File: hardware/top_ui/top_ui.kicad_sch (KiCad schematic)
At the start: 25 parts, among them J1 USB-C, J2 J_STK_A, J3 J_STK_B, J5 ST7789 240x280, J6 Stern Klinke, J7 Reserve UART, Q1 BC847, Q2 P-FET 20V 1A, SW1 BTN1, SW2 BTN2, SW3 BTN3, SW4 BTN4, U1 USBLC6-2SC6, U2 SHT40-AD1B, U3 VL53L1X

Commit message: USB-C wandert auf das Mid-Board, Top bekommt eine Randkerbe
Der Grund ist Bauhoehe, nicht Routing. Ueber dem Top-Board sind bis zur
Zentralscheibe 3,5 mm frei; eine stehende USB-C-Buchse baut 7 bis 9,25 mm
(GCT USB4115: H = 9,25 mm laut Datenblatt). Sie haette die Scheibe
durchstossen. Zwischen Mids und Tops Oberseite liegen dagegen 10,0 mm.

Die Buchse steht jetzt auf Mid bei (3,5 / 20,3) und greift durch eine offene
Randkerbe des Top-Boards nach vorn - gesteckt wird weiterhin frontal, sobald
die Zentralscheibe ab ist. Koerper 8,3 x 4,3 mm, Kerbe 11,0 mm breit ab
y = 16,8 bis zum Rand.

Offene Kerbe statt Fenster, weil der Boardrand bei y = 23,5 liegt: Ein
geschlossenes Fenster liesse einen Steg von einem halben Millimeter stehen,
der beim Nutzentrennen bricht.

MITGEWANDERT sind die ESD-Diode (U5) und die beiden CC-Widerstaende
(R18/R19). Damit verlieren USB_DP und USB_DN ihren Weg durch den Stapel:
J_STK_A 34/36 heissen jetzt RSV_A3/RSV_A5. Der native USB des ESP32-S3 sitzt
auf demselben Board wie die Buchse. Stack-Pinout auf v0.4.

USB_VBUS bleibt auf A18 - es geht weiter nach unten zum Power-Mux auf Bottom,
kommt jetzt nur von Mid statt von Top.

PLATZIERUNG. Der Bodenrand von Mid war belegt: RS485 (J4) nach links auf
(-11,5 / 19,0) gerueckt, PhotoMOS (U4) aus der Fixliste genommen. Ein
Rastersuchlauf ueber beide Seiten fand fuer U4 keine freie Flaeche von
11,6 x 3,6 mm - der automatische Platzierer bringt ihn jetzt selbst unter und
hat ihn nach (-20,1 / 7,9) gelegt. Oben ging es nicht, dort steht das
ESP32-Modul mit seiner Antenne; links und rechts laesst Tops Displayfenster
nur 7,2 mm Rand.

inside_outline() kennt die Kerbe, der Platzierer legt dort nichts ab, und der
Zonenumriss folgt ihr.

  top_ui     27 -> 21 Bauteile, unrouted 63 -> 48
  mid_logic  46 -> 50 Bauteile

Co-Authored-By: Claude Opus 5 (1M context) <noreply@anthropic.com>
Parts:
- removed J1: USB-C, Connector_USB:USB_C_Receptacle_G-Switch_GT-USB-7051x, symbol Connector:USB_C_Receptacle_USB2.0_16P
- removed R1, R2: 5k1, Resistor_SMD:R_0603_1608Metric, symbol Device:R
- removed U1: USBLC6-2SC6, Package_TO_SOT_SMD:SOT-23-6, symbol Power_Protection:USBLC6-2SC6
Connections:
- net USB_DN renamed RSV_A5
- net USB_DP renamed RSV_A3
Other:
- moved on the sheet: C1, C2, C3, C4, F1, J2, J3, J5, J6, J7, Q1, Q2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

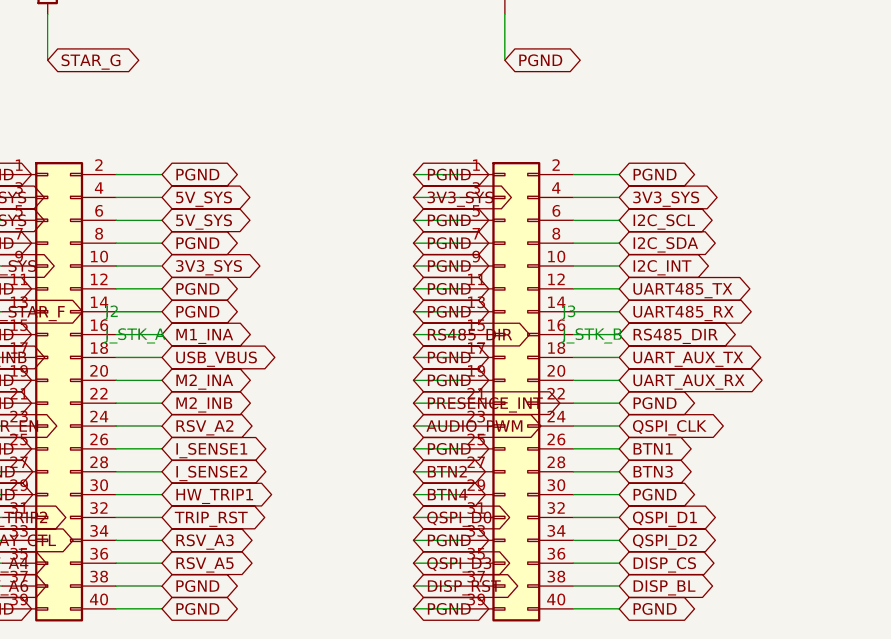
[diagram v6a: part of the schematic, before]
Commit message: Stack-Pinout v0.5: Tasten und I2C auf die Aussenreihe, Tasten auf beide Verbinder
Zwei Autorouter (1.9.0 und 2.3.0) und zwei Lagenzahlen hatten auf Top exakt
dieselben elf offenen Netze hinterlassen. Das ist kein Werkzeugproblem,
sondern die Pinbelegung.

BTN1..BTN4 lagen auf B26..B29 - vier benachbarten Kontakten der INNENreihe
des RECHTEN Verbinders. Ihre Taster sitzen aber in allen vier Ecken des
Top-Boards, zwei davon links. Zwei Bahnen mussten quer ueber ein Board mit
80 Steckkontakten im 1,27-mm-Raster, und alle vier zuerst aus der Innenreihe
heraus. I2C_SCL/SDA lagen ebenfalls innen.

Neu liegt jedes Tastennetz auf der AUSSENreihe des Verbinders, der seiner
Ecke am naechsten ist - von dort geht es direkt nach aussen und am Boardrand
entlang zum Taster:

  BTN1  B26 -> B1    aussen, y = -14,06   SW1 (+18 / -20)
  BTN2  B27 -> A2    aussen, y = -14,06   SW2 (-18 / -20)
  BTN3  B28 -> A40   aussen, y = +10,07   SW3 (-18 / +20)
  BTN4  B29 -> B39   aussen, y = +10,07   SW4 (+18 / +20)

  I2C_SCL  B6 -> B5  aussen
  I2C_SDA  B8 -> B7  aussen

Beide I2C-Teilnehmer auf Top - SHT4x und ToF - sitzen an der oberen Kante,
also dort, wo die neuen Pins liegen.

Die freigewordenen Kontakte B6, B8, B26..B29 werden PGND. Vier PGND-Pins sind
weggefallen (A2, A40, B1, B39); ueber beide Verbinder bleiben 25.

Alle drei Schaltplaene und Layouts neu erzeugt, Netzlistenvergleich bestanden,
keine Platzierungsfehler. Das Routing folgt.

Co-Authored-By: Claude Opus 5 (1M context) <noreply@anthropic.com>
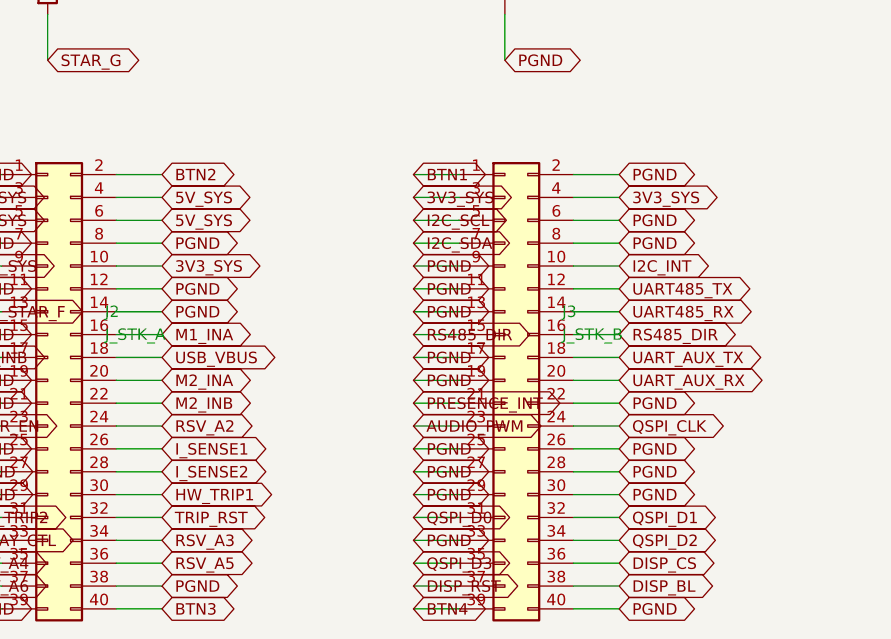
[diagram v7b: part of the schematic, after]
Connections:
- net BTN1: now also J3.1 (Pin_1); no longer J3.26 (Pin_26)
- net BTN2: now also J2.2 (Pin_2); no longer J3.27 (Pin_27)
- net BTN3: now also J2.40 (Pin_40); no longer J3.28 (Pin_28)
- net BTN4: now also J3.39 (Pin_39); no longer J3.29 (Pin_29)
- net I2C_SCL: now also J3.5 (Pin_5); no longer J3.6 (Pin_6)
- net I2C_SDA: now also J3.7 (Pin_7); no longer J3.8 (Pin_8)
- net PGND: now also J3.26 (Pin_26), J3.27 (Pin_27), J3.28 (Pin_28), J3.29 (Pin_29), J3.6 (Pin_6), J3.8 (Pin_8); no longer J2.2 (Pin_2), J2.40 (Pin_40), J3.1 (Pin_1), J3.39 (Pin_39), J3.5 (Pin_5), J3.7 (Pin_7)

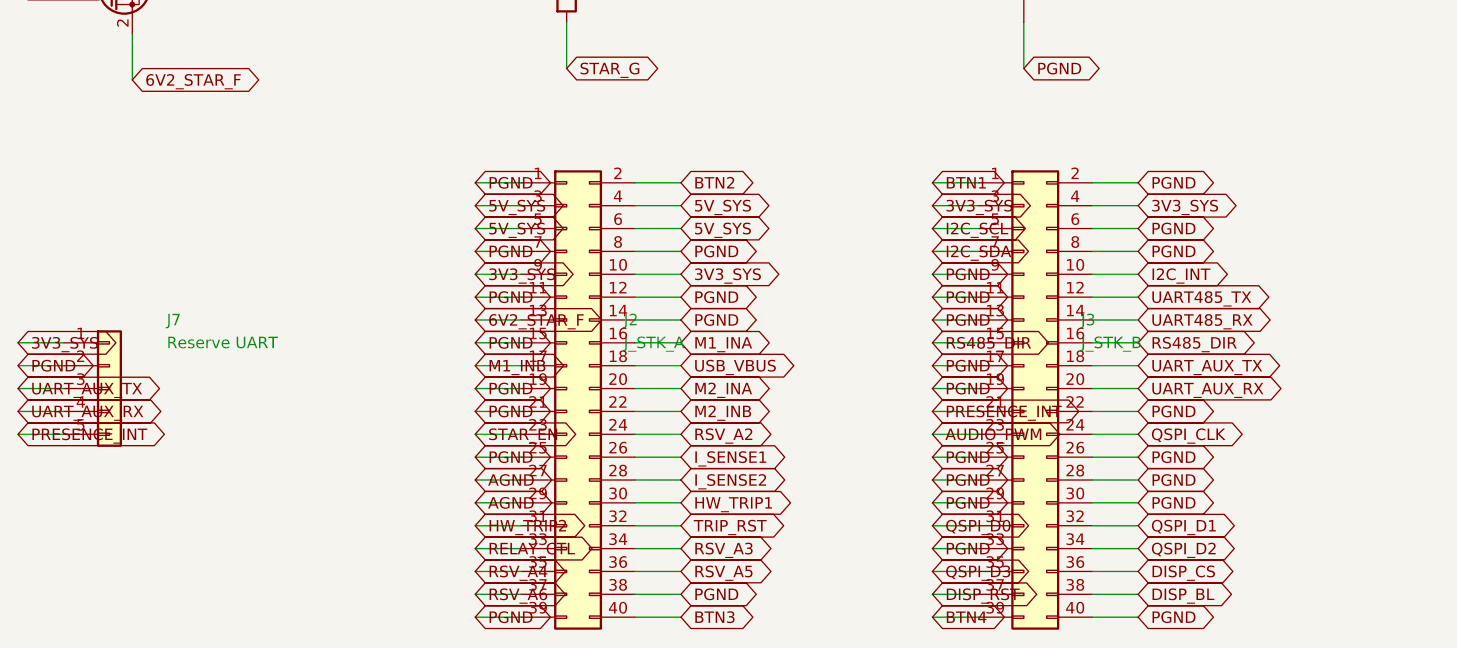
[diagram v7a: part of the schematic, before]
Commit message: docs/16: Anleitung fuer die letzten Handgriffe in KiCad
Was der Autorouter uebrig laesst, ist wenig und immer dasselbe Muster: Pads,
die zwischen anderen Bauteilen eingeklemmt sind. Die Anleitung nennt die
Tastenkuerzel (X fuer Bahn, V fuer Lagenwechsel mit Via, B fuer Zonen
fuellen), den aktuellen Stand je Board als Anhaltspunkt und die
Reihenfolge danach - Zonen fuellen VOR der DRC, sonst sucht man Fehler, die
keine sind.

Dazu zwei Warnungen: keine Bauteile verschieben, die Positionen kommen aus
gen_layouts.py und gehen beim naechsten Neuerzeugen verloren. Und die Regeln
nicht lockern - wenn die DRC meckert, ist die Bahn falsch.

Co-Authored-By: Claude Opus 5 (1M context) <noreply@anthropic.com>
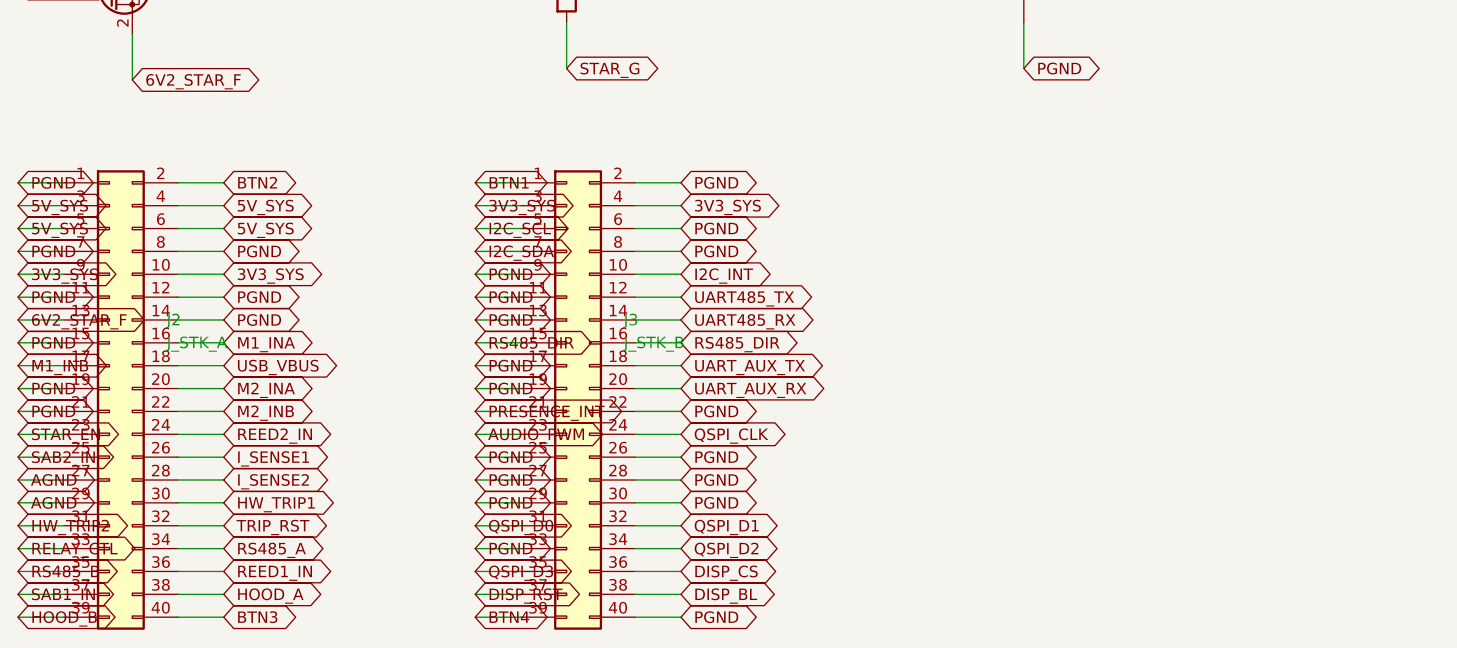
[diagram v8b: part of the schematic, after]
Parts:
- removed J7: Reserve UART, Connector_JST:JST_PH_B5B-PH-K_1x05_P2.00mm_Vertical, symbol Connector_Generic:Conn_01x05
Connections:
- net PGND: no longer J2.25 (Pin_25), J2.38 (Pin_38), J2.39 (Pin_39)
- net RSV_A2 renamed REED2_IN
- net RSV_A3 renamed RS485_A
- net RSV_A4 renamed RS485_B
- net RSV_A5 renamed REED1_IN
- net RSV_A6 renamed SAB1_IN
- new net HOOD_A: J2.38 (Pin_38)
- new net HOOD_B: J2.39 (Pin_39)
- new net SAB2_IN: J2.25 (Pin_25)
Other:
- moved on the sheet: J2, J3
